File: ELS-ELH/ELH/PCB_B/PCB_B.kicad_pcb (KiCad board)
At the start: 2 copper layers, 95 x 95 mm, 22 parts, among them J1 Pressure Transducer Input, J3 Conn_01x20_Pin, J4 Conn_01x20_Pin, U1 GY-87

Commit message: PCB B connection advances
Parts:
- removed GPS1: Ublox Neo-6m, ELH_Library:Ublox Neo-6m
- J1: footprint TerminalBlock:TerminalBlock_MaiXu_MX126-5.0-03P_1x03_P5.00mm -> ELH_Library:Bornera 3P
- R12: moved to F.Cu
- R5: moved to B.Cu
- moved J4 96.8 mm to (24.1, 44.0), turned to -90 degrees
- moved J3 84.0 mm to (-24.1, -44.0)
- moved BZ1 73.0 mm to (-9.90, 33.9)
- moved R7 71.9 mm to (-29.0, -22.0), turned to -90 degrees
- moved R4 68.0 mm to (-35.6, -22.1), turned to -90 degrees
- moved D10 61.3 mm to (-39.3, -7.82), turned to 0 degrees
- moved W25QXX1 57.8 mm to (4.21, 23.7), turned to 0 degrees
- moved U1 50.2 mm to (-6.50, -35.1)
- moved C2 37.9 mm to (-28.3, -33.3)
- moved C13 36.3 mm to (-35.3, -36.0)
- moved R12 30.8 mm to (-10.1, 24.1), turned to 0 degrees
- moved SD_Adapter1 26.8 mm to (19.2, -35.8)
- moved BME2 19.5 mm to (37.8, -16.2)
- moved R5 11.8 mm to (-32.3, -22.1), turned to -90 degrees
- moved J1 5.20 mm to (-36.6, 7.70)
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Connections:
- ADC1 pad 1: unconnected-(ADC1-A3-Pad1) -> /PT_ADC1
- ADC1 pad 4: /PT_ADC1 -> unconnected-(ADC1-A0-Pad4)
- Adapter1 pad 10: /LED1 -> /LED3
- Adapter1 pad 12: /LED3 -> /LED1
- Bornera7 pad 1: /UART2_TX_1 -> /UART2_TX_2
- Bornera7 pad 2: /UART2_RX_1 -> /UART2_RX_2
- Converter1 pad 12: /I2C1_SCL -> /I2C1_SDA
- Converter1 pad 13: /I2C1_SDA -> /I2C1_SCL
- Converter1 pad 14: /UART2_RX_2 -> /UART2_TX_2
- Converter1 pad 15: /UART2_TX_2 -> /UART2_RX_2
- Converter1 pad 2: /I2C1_SCL_1 -> /I2C1_SDA_1
- Converter1 pad 3: /I2C1_SDA_1 -> /I2C1_SCL_1
- Converter1 pad 4: /UART2_RX_1 -> /UART2_TX_1
- Converter1 pad 5: /UART2_TX_1 -> /UART2_RX_1
- ESP1 pad 10: /SPI2_MISO -> unconnected-(ESP1-D27-Pad10)
- ESP1 pad 17: GND -> unconnected-(ESP1-GND-Pad17)
- ESP1 pad 18: /CS_FLASH -> unconnected-(ESP1-D15-Pad18)
- ESP1 pad 20: /CS_IMURaw -> unconnected-(ESP1-D4-Pad20)
- ESP1 pad 21: /SPI2_SCK -> /SPI2_MOSI
- ESP1 pad 22: /SPI2_MOSI -> /SPI2_MISO
- ESP1 pad 23: unconnected-(ESP1-D5-Pad23) -> /SPI2_SCK
- ESP1 pad 27: unconnected-(ESP1-RX0-Pad27) -> /SPI1_MOSI
- ESP1 pad 28: unconnected-(ESP1-TX0-Pad28) -> /CS_ALT
- ESP1 pad 30: /SPI1_MOSI -> /CS_FLASH
- ESP1 pad 7: /CS_ALT -> unconnected-(ESP1-D33-Pad7)
- J3 pad 1: GND -> unconnected-(J3-Pin_1-Pad1)
- J3 pad 14: unconnected-(J3-Pin_14-Pad14) -> /UART1_RX_2
- J3 pad 15: unconnected-(J3-Pin_15-Pad15) -> /UART1_RX_2
- J3 pad 16: unconnected-(J3-Pin_16-Pad16) -> /UART1_RX_2
- J3 pad 17: unconnected-(J3-Pin_17-Pad17) -> /UART1_TX_2
- J3 pad 18: unconnected-(J3-Pin_18-Pad18) -> /UART1_TX_2
- J3 pad 19: unconnected-(J3-Pin_19-Pad19) -> /UART1_TX_2
- J3 pad 2: /UART1_RX_2 -> unconnected-(J3-Pin_2-Pad2)
- J3 pad 20: unconnected-(J3-Pin_20-Pad20) -> GND
- J3 pad 3: /UART1_RX_2 -> unconnected-(J3-Pin_3-Pad3)
- J3 pad 4: /UART1_RX_2 -> unconnected-(J3-Pin_4-Pad4)
- J3 pad 5: /UART1_TX_2 -> unconnected-(J3-Pin_5-Pad5)
- J3 pad 6: /UART1_TX_2 -> unconnected-(J3-Pin_6-Pad6)
- J3 pad 7: /UART1_TX_2 -> unconnected-(J3-Pin_7-Pad7)
- J4 pad 12: unconnected-(J4-Pin_12-Pad12) -> GND
- J4 pad 15: unconnected-(J4-Pin_15-Pad15) -> /UART3_RX
- J4 pad 16: unconnected-(J4-Pin_16-Pad16) -> /UART3_TX
- U1 pad 4: /I2C1_SCL_1 -> /I2C1_SCL
- U1 pad 5: /I2C1_SDA_1 -> /I2C1_SDA
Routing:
- net +3.3V: track 0.00 -> 323.0 mm, vias 0 -> 2
- net +5V: track 0.00 -> 221.4 mm, vias 0 -> 2
- net /I2C1_SCL: track 0.00 -> 170.7 mm
- net /UART2_RX_1: track 0.00 -> 148.0 mm
- net /I2C1_SDA: track 0.00 -> 145.1 mm, vias 0 -> 1
- net /UART2_TX_1: track 0.00 -> 127.0 mm
- net /I2C1_SDA_1: track 0.00 -> 119.7 mm
- net /I2C1_SCL_1: track 0.00 -> 117.5 mm
- net /CS_SD: track 0.00 -> 81.8 mm
- net /UART2_TX_2: track 0.00 -> 66.4 mm
- net /UART1_RX_2: track 0.00 -> 65.4 mm, vias 0 -> 1
- net /MOS1_2: track 0.00 -> 64.7 mm
- net /UART2_RX_2: track 0.00 -> 63.2 mm
- net /UART1_TX_2: track 0.00 -> 61.7 mm, vias 0 -> 1
- net /SPI1_SCK: track 0.00 -> 56.1 mm
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- added copper zone on B.Cu, net GND
- added copper zone on F.Cu, net GND
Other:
- outline, holes or cut-outs redrawn
- board text added: "D1"

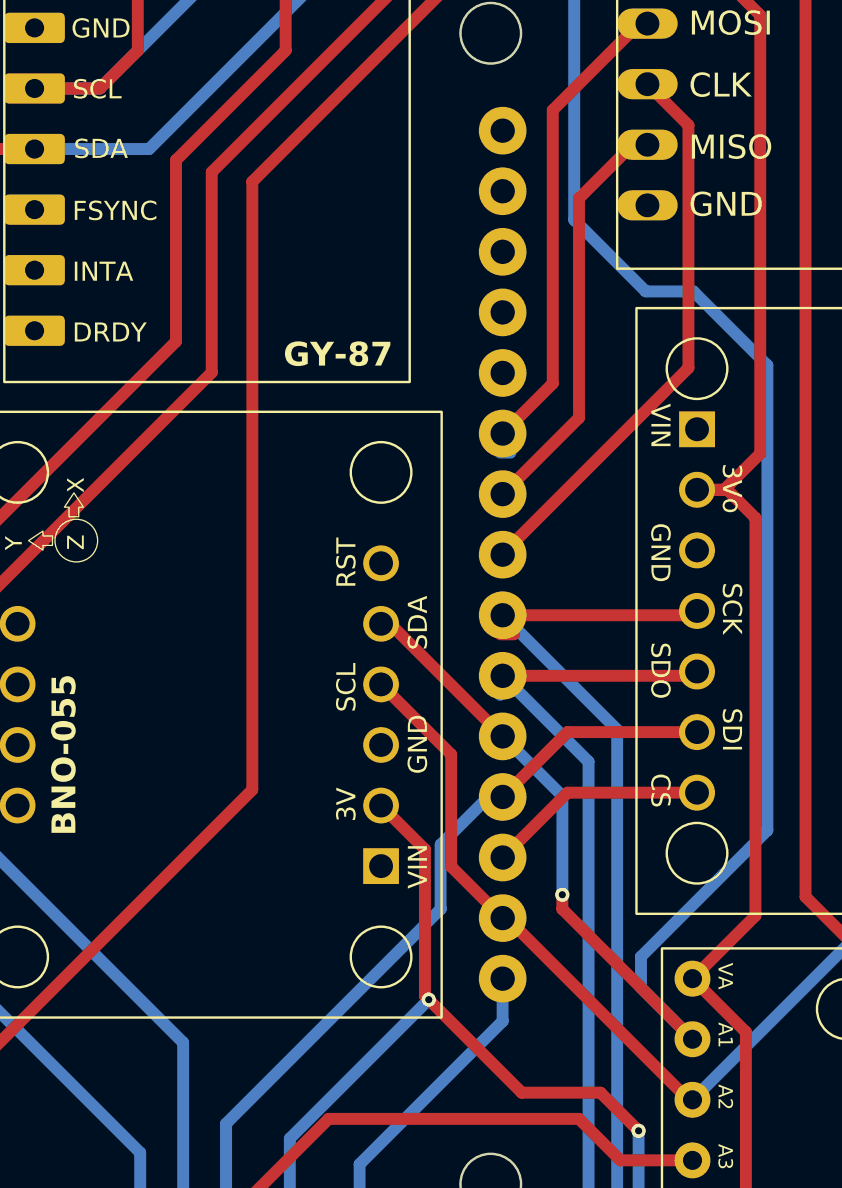
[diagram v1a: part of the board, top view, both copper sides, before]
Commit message: modified I2C bus
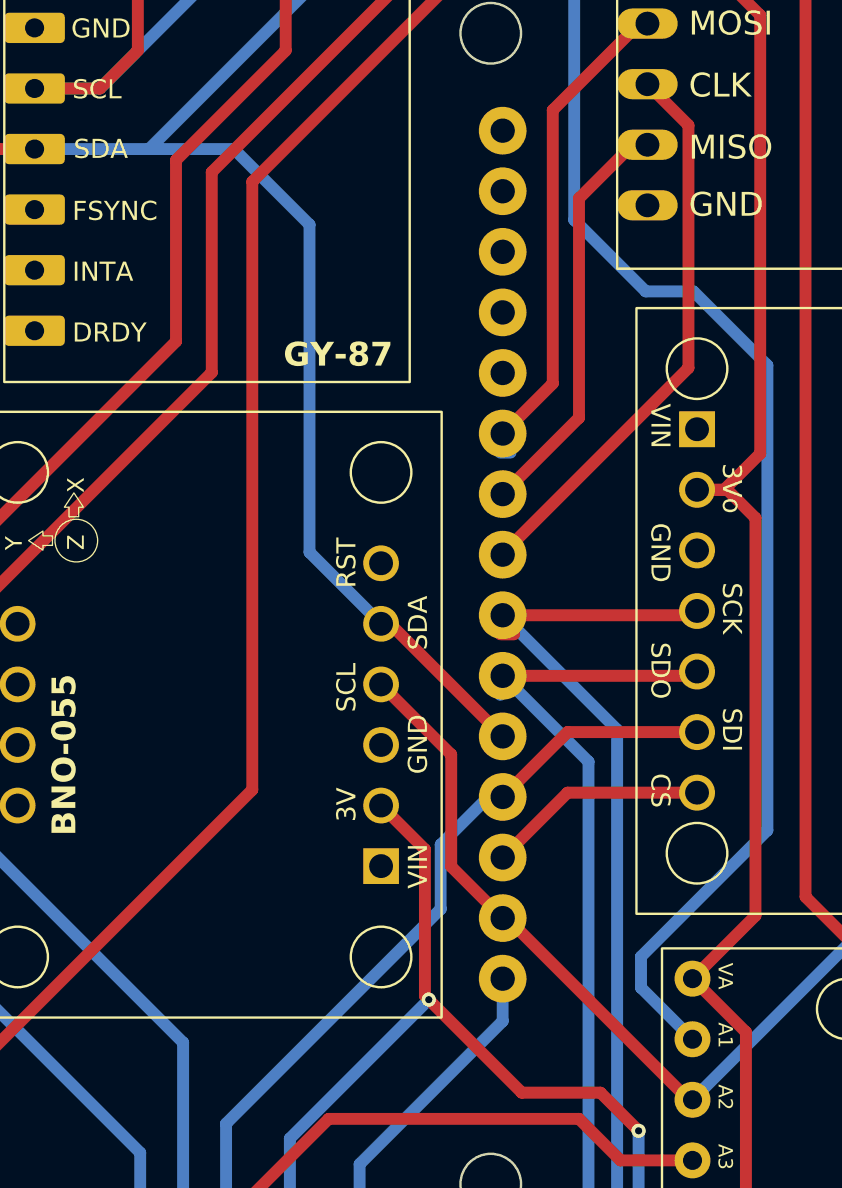
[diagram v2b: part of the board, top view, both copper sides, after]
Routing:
- net /I2C1_SDA: track 145.1 -> 155.1 mm, vias 1 -> 0
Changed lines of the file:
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@@
-	)
-	(segment
-		(start 16.9 8.4)
-		(end 16.9 9)
-		(width 0.5)
-		(layer "F.Cu")
-		(net 31)
 	)
 	(segment
@@
 	)
 	(segment
-		(start 16.9 9)
-		(end 22.36 14.46)
-		(width 0.5)
-		(layer "F.Cu")
-		(net 31)
-	)
-	(via
-		(at 16.9 8.4)
-		(size 0.6)
-		(drill 0.3)
-		(layers "F.Cu" "B.Cu")
-		(net 31)
-	)
-	(segment
 		(start 20.2 12.3)
 		(end 20.2 11)
@@
 		(start 25.5 5.7)
 		(end 25.5 -13.8)
+		(width 0.5)
+		(layer "B.Cu")
+		(net 31)
+	)
+	(segment
+		(start -0.43 -22.87)
+		(end 3.13 -22.87)
 		(width 0.5)
 		(layer "B.Cu")
@@
 	)
 	(segment
-		(start 16.9 4.26)
-		(end 16.9 8.4)
+		(start 3.13 -22.87)
+		(end 6.3 -19.7)
+		(width 0.5)
+		(layer "B.Cu")
+		(net 31)
+	)
+	(segment
+		(start 6.3 -5.96)
+		(end 9.3 -2.96)
 		(width 0.5)
 		(layer "B.Cu")
@@
 	)
 	(segment
-		(start 14.4 1.76)
-		(end 16.9 4.26)
+		(start 6.3 -19.7)
+		(end 6.3 -5.96)
 		(width 0.5)
 		(layer "B.Cu")

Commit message: final updates
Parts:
- added J2: Conn_01x04_Pin, Connector_PinSocket_2.54mm:PinSocket_1x04_P2.54mm_Vertical, F.Cu at (0.10, 18.2)
- moved R12 1.56 mm to (-11.2, 25.2)
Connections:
- Bornera7 pad 1: /UART2_TX_2 -> /UART2_TX_1
- Bornera7 pad 2: /UART2_RX_2 -> /UART2_RX_1
- C13 pad 1: +5V -> +5VA
- C2 pad 2: +5V -> +5VA
- Converter1 pad 12: /I2C1_SDA -> /I2C1_SCL
- Converter1 pad 13: /I2C1_SCL -> /I2C1_SDA
- Converter1 pad 2: /I2C1_SDA_1 -> /I2C1_SCL_1
- Converter1 pad 3: /I2C1_SCL_1 -> /I2C1_SDA_1
- ESP1 pad 15: +5V -> +5VA
- ESP1 pad 5: /UART2_RX_1 -> /UART2_RX_2
- ESP1 pad 9: /UART2_TX_1 -> /UART2_TX_2
- J3 pad 10: unconnected-(J3-Pin_10-Pad10) -> +5V
- J3 pad 11: unconnected-(J3-Pin_11-Pad11) -> /UART1_RX_2
- J3 pad 12: unconnected-(J3-Pin_12-Pad12) -> /UART1_RX_2
- J3 pad 13: unconnected-(J3-Pin_13-Pad13) -> /UART1_RX_2
- J3 pad 14: /UART1_RX_2 -> GND
- J3 pad 15: /UART1_RX_2 -> GND
- J3 pad 16: /UART1_RX_2 -> GND
- J3 pad 2: unconnected-(J3-Pin_2-Pad2) -> +5VA
- J3 pad 3: unconnected-(J3-Pin_3-Pad3) -> +5VA
- J3 pad 4: unconnected-(J3-Pin_4-Pad4) -> +5VA
- J3 pad 5: unconnected-(J3-Pin_5-Pad5) -> +3.3V
- J3 pad 6: unconnected-(J3-Pin_6-Pad6) -> +3.3V
- J3 pad 7: unconnected-(J3-Pin_7-Pad7) -> +3.3V
- J3 pad 8: unconnected-(J3-Pin_8-Pad8) -> +5V
- J3 pad 9: unconnected-(J3-Pin_9-Pad9) -> +5V
- J4 pad 10: unconnected-(J4-Pin_10-Pad10) -> /MOS1_2
- J4 pad 11: unconnected-(J4-Pin_11-Pad11) -> +3.3V
- J4 pad 12: GND -> +3.3V
- J4 pad 14: +5V -> +5VA
- J4 pad 15: /UART3_RX -> +5VA
- J4 pad 16: /UART3_TX -> +5VA
- J4 pad 17: unconnected-(J4-Pin_17-Pad17) -> GND
- J4 pad 2: unconnected-(J4-Pin_2-Pad2) -> GND
- J4 pad 3: unconnected-(J4-Pin_3-Pad3) -> GND
- J4 pad 4: unconnected-(J4-Pin_4-Pad4) -> GND
- J4 pad 5: unconnected-(J4-Pin_5-Pad5) -> +5V
- J4 pad 6: unconnected-(J4-Pin_6-Pad6) -> +5V
- J4 pad 7: /MOS1_2 -> +5V
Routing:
- net +5VA: track 0.00 -> 156.8 mm, vias 0 -> 2
- net /UART2_RX_1: track 148.0 -> 0.00 mm
- net /UART2_TX_1: track 127.0 -> 0.08 mm
- net /UART2_RX_2: track 63.2 -> 145.0 mm
- net /UART2_TX_2: track 66.4 -> 126.8 mm
- net +3.3V: track 323.0 -> 353.8 mm, vias 2 -> 0
- net /UART3_TX: track 56.0 -> 27.1 mm, vias 1 -> 0
- net /UART3_RX: track 43.5 -> 20.6 mm, vias 1 -> 0
- net /I2C1_SCL: track 170.7 -> 192.2 mm
- net +5V: track 221.4 -> 204.0 mm, vias 2 -> 1
- net /I2C1_SDA_1: track 119.7 -> 126.4 mm
- net GND: track 0.00 -> 5.08 mm
- net Net-(BZ1-+): track 12.9 -> 11.3 mm
- net /I2C1_SDA: track 155.1 -> 156.6 mm
- net /UART1_RX_2: track 65.4 -> 64.6 mm

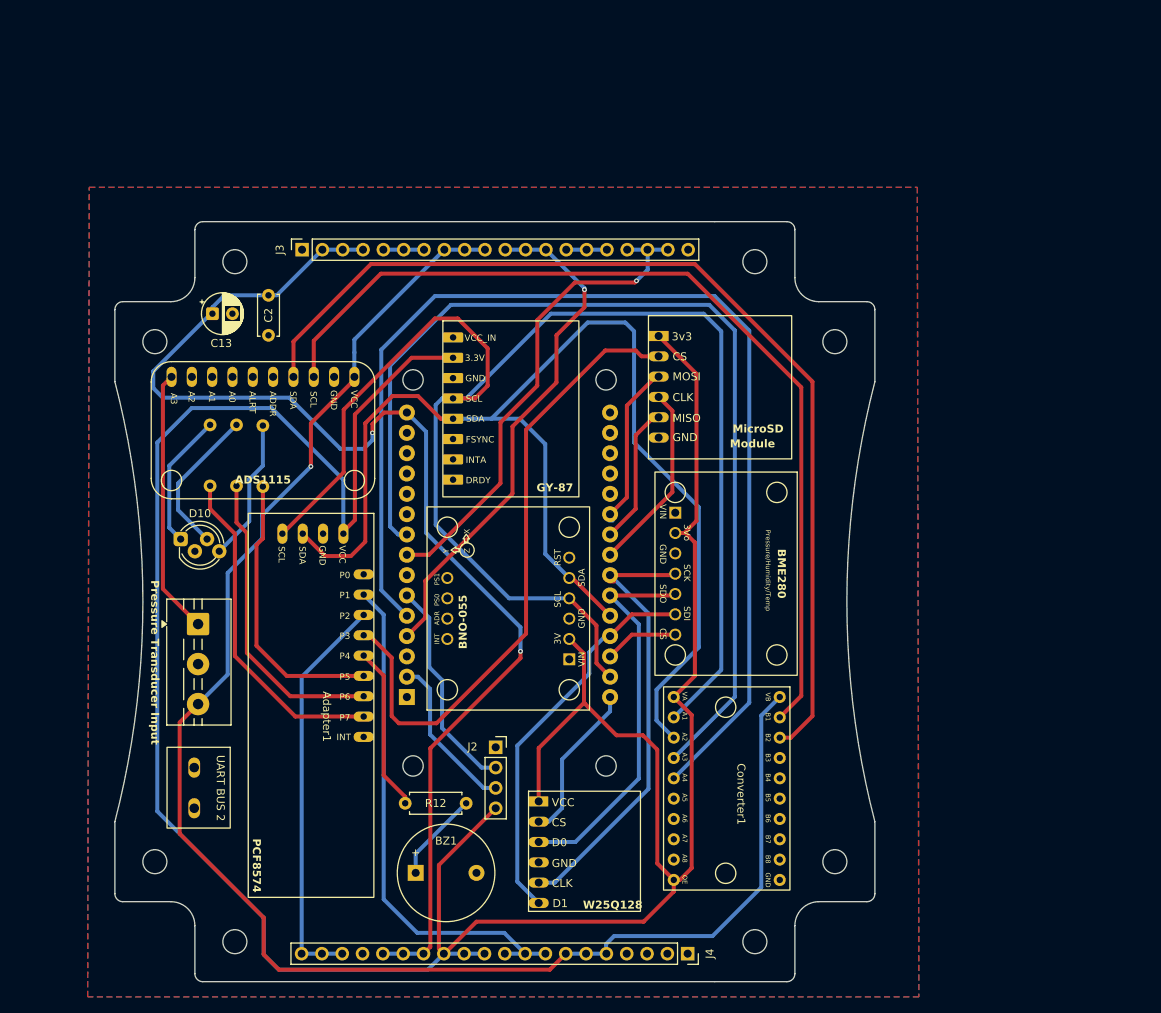
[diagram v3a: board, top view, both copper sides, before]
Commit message: PCB B reorganized
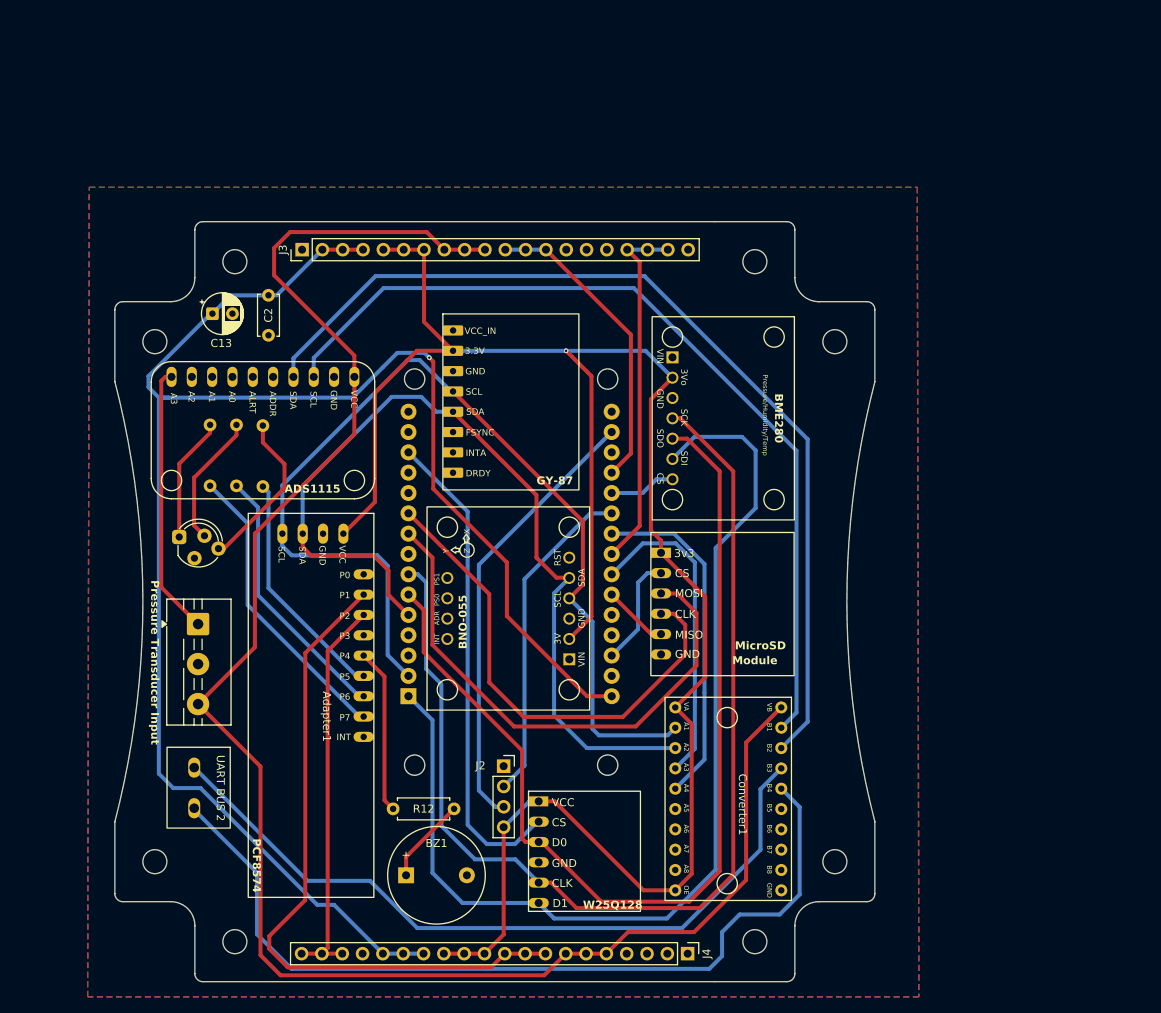
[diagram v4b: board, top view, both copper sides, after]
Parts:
- D10: footprint LED_THT:LED_D5.0mm-4_RGB_Staggered_Pins -> ELH_Library:LED RGB
- J3, J4: footprint Connector_PinSocket_2.54mm:PinSocket_1x20_P2.54mm_Vertical -> Connector_PinHeader_2.54mm:PinHeader_1x20_P2.54mm_Vertical
- moved SD_Adapter1 27.1 mm to (19.5, -8.65)
- moved BME2 19.4 mm to (37.4, -35.6)
- moved J2 2.56 mm to (1.10, 20.6)
- moved D10 1.73 mm to (-37.6, -7.74)
- moved R12 1.66 mm to (-12.7, 25.9)
- moved Converter1 1.31 mm to (37.1, 11.9)
- moved BZ1 1.24 mm to (-11.1, 34.2)
- moved U1 0.87 mm to (-6.50, -36.0)
- moved ESP1 0.23 mm to (1.40, -3.70)
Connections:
- Adapter1 pad 8: /CS_SD -> unconnected-(Adapter1-P3-Pad8)
- ESP1 pad 10: unconnected-(ESP1-D27-Pad10) -> /SPI2_MISO
- ESP1 pad 13: unconnected-(ESP1-D13-Pad13) -> /CS_SD
- ESP1 pad 18: unconnected-(ESP1-D15-Pad18) -> /CS_FLASH
- ESP1 pad 21: /SPI2_MOSI -> /SPI2_SCK
- ESP1 pad 22: /SPI2_MISO -> /SPI2_MOSI
- ESP1 pad 23: /SPI2_SCK -> unconnected-(ESP1-D5-Pad23)
- ESP1 pad 27: /SPI1_MOSI -> unconnected-(ESP1-RX0-Pad27)
- ESP1 pad 28: /CS_ALT -> unconnected-(ESP1-TX0-Pad28)
- ESP1 pad 30: /CS_FLASH -> /SPI1_MOSI
- ESP1 pad 5: /UART2_RX_2 -> /CS_ALT
- ESP1 pad 7: unconnected-(ESP1-D33-Pad7) -> /UART2_RX_2
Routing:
- net +3.3V: track 353.8 -> 238.3 mm, vias 0 -> 1
- net /UART2_RX_1: track 0.00 -> 108.4 mm
- net /UART2_RX_2: track 145.0 -> 43.6 mm
- net /UART2_TX_1: track 0.08 -> 94.4 mm
- net /UART2_TX_2: track 126.8 -> 39.8 mm
- net /SPI1_MOSI: track 48.9 -> 130.3 mm
- net /SPI1_SCK: track 56.1 -> 137.1 mm
- net /SPI1_MISO: track 48.4 -> 123.5 mm
- net /CS_SD: track 81.8 -> 13.9 mm
- net /I2C1_SCL: track 192.2 -> 128.0 mm
- net +5VA: track 156.8 -> 217.2 mm, vias 2 -> 1
- net /SPI2_MOSI: track 20.3 -> 67.6 mm
- net /I2C1_SDA: track 156.6 -> 113.0 mm
- net /CS_FLASH: track 20.0 -> 60.7 mm
- net /SPI2_SCK: track 23.8 -> 62.1 mm
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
